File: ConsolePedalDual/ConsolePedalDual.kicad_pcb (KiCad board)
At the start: 2 copper layers, 92.3 x 90.2 mm, 14 parts, among them J1 AudioJack3, J2 AudioJack2, J3 Conn_02x25_Odd_Even, J4 Conn_02x25_Odd_Even, SW1 Bypass

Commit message: Finished schematic. Trying to figure out how to fit all these components on this board
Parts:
- removed SW1: Bypass, Connector_PinSocket_2.54mm:PinSocket_1x02_P2.54mm_Vertical
- added C1: 47uF, Capacitor_THT:CP_Radial_D6.3mm_P2.50mm, F.Cu at (232.5, 67.9)
- added C2: 2.2uF, Capacitor_THT:CP_Radial_D4.0mm_P2.00mm, F.Cu at (174.4, 78.7)
- added C3: 2.2uF, Capacitor_THT:CP_Radial_D4.0mm_P2.00mm, F.Cu at (186.2, 56.6)
- added C4: 2.2uF, Capacitor_THT:CP_Radial_D4.0mm_P2.00mm, F.Cu at (174.4, 86.0)
- added C5: 2.2uF, Capacitor_THT:CP_Radial_D4.0mm_P2.00mm, F.Cu at (186.2, 64.0)
- added C6: 2.2uF, Capacitor_THT:CP_Radial_D4.0mm_P2.00mm, F.Cu at (196.4, 71.3)
- added C7: 2.2uF, Capacitor_THT:CP_Radial_D4.0mm_P2.00mm, F.Cu at (208.1, 56.6)
- added R2: 10K, Resistor_THT:R_Axial_DIN0207_L6.3mm_D2.5mm_P10.16mm_Horizontal, F.Cu at (121.7, 94.2)
- added R3: 10K, Resistor_THT:R_Axial_DIN0207_L6.3mm_D2.5mm_P10.16mm_Horizontal, F.Cu at (207.7, 61.9)
- added R4: 510K, Resistor_THT:R_Axial_DIN0207_L6.3mm_D2.5mm_P10.16mm_Horizontal, F.Cu at (217.9, 66.0)
- added R5: 510K, Resistor_THT:R_Axial_DIN0207_L6.3mm_D2.5mm_P10.16mm_Horizontal, F.Cu at (221.1, 61.9)
- added R6: 510K, Resistor_THT:R_Axial_DIN0207_L6.3mm_D2.5mm_P10.16mm_Horizontal, F.Cu at (209.3, 76.6)
- added R7: 510K, Resistor_THT:R_Axial_DIN0207_L6.3mm_D2.5mm_P10.16mm_Horizontal, F.Cu at (196.0, 80.7)
- added R8: 510K, Resistor_THT:R_Axial_DIN0207_L6.3mm_D2.5mm_P10.16mm_Horizontal, F.Cu at (196.0, 84.7)
- added R9: 510K, Resistor_THT:R_Axial_DIN0207_L6.3mm_D2.5mm_P10.16mm_Horizontal, F.Cu at (217.9, 70.0)
- added U1: CD4053B, Package_DIP:DIP-16_W7.62mm_Socket, F.Cu at (133.3, 55.5)
- J3: value Conn_02x25_Odd_Even -> Slot A
- J4: value Conn_02x25_Odd_Even -> Slot B
- R1: value R -> LED
- moved D2 23.7 mm to (125.2, 94.0), turned to 90 degrees
- moved J2 13.3 mm to (157.7, 91.2)
- moved J1 12.6 mm to (117.3, 88.1)
- moved BT1 12.4 mm to (117.3, 79.8)
- moved D1 8.38 mm to (137.2, 77.1)
- moved R1 1.40 mm to (142.2, 83.3)
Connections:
- J3 pad 10: +9V -> /SlotA
- J3 pad 42: +9V -> /SlotA
- J3 pad 43: /SecondFX -> /SlotAOutput
- J3 pad 44: /SecondFX -> /SlotAOutput
- J3 pad 45: /Input -> /SlotAInput
- J3 pad 46: /Input -> /SlotAInput
- J3 pad 5: /Input -> /SlotAInput
- J3 pad 6: /Input -> /SlotAInput
- J3 pad 7: /SecondFX -> /SlotAOutput
- J3 pad 8: /SecondFX -> /SlotAOutput
- J4 pad 10: +9V -> /SlotB
- J4 pad 42: +9V -> /SlotB
- J4 pad 45: /SecondFX -> /SlotBInput
- J4 pad 46: /SecondFX -> /SlotBInput
- J4 pad 5: /SecondFX -> /SlotBInput
- J4 pad 6: /SecondFX -> /SlotBInput
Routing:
- net /LEDPower: track 155.5 -> 0.62 mm
- net +9V: track 147.9 -> 0.00 mm
- net /Output: track 144.2 -> 0.00 mm
- net /Input: track 131.0 -> 0.00 mm
- net /SecondFX: track 123.7 -> 0.00 mm
- net Net-(J1-Pad3): track 30.6 -> 0.00 mm
- net GND: track 30.5 -> 0.00 mm
- net Net-(J2-Pad1): track 23.4 -> 0.00 mm
- net Net-(D1-Pad1): track 16.6 -> 0.00 mm
- net Net-(BT1-Pad1): track 14.7 -> 0.00 mm
- net Net-(BT1-Pad2): track 9.33 -> 0.00 mm
- net Net-(S1-PadP$1): track 5.30 -> 0.00 mm

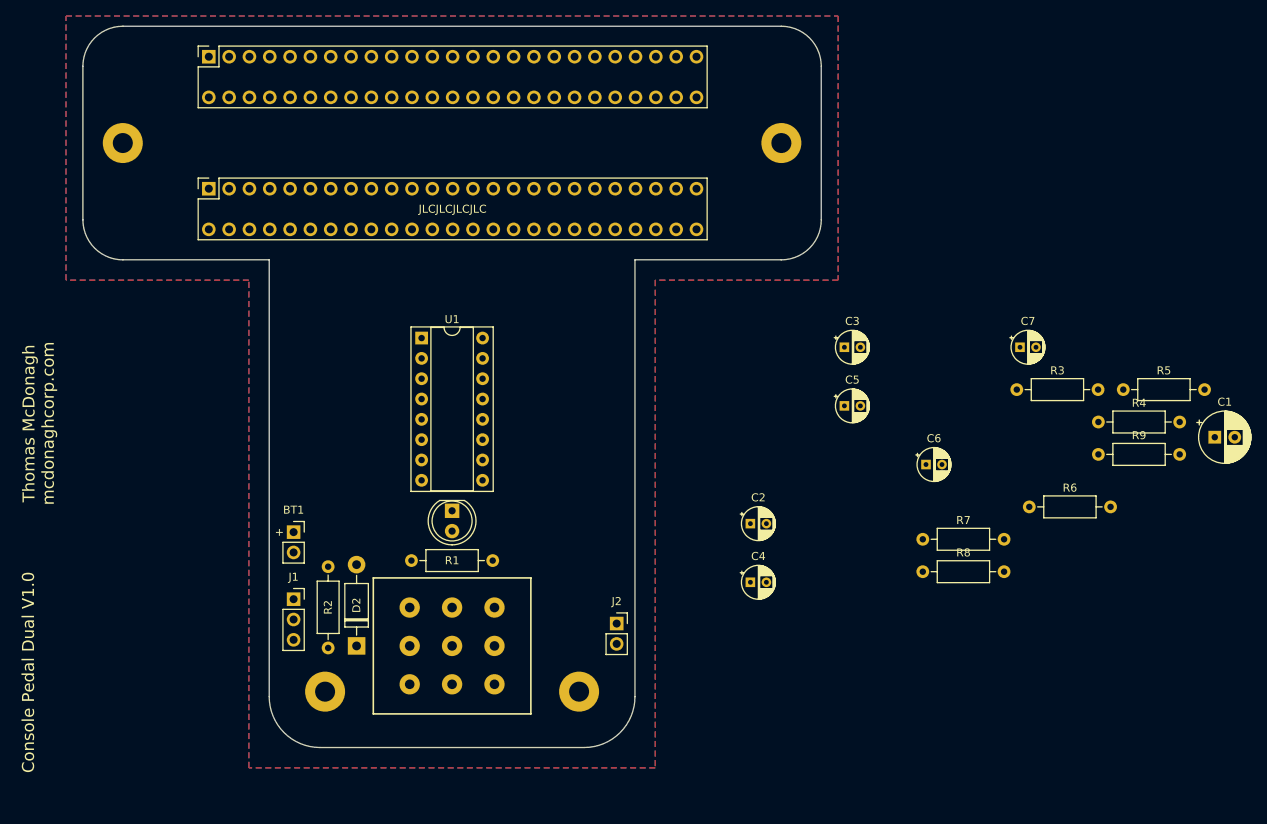
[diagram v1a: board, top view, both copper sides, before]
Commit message: Figured out how to fit components on board. Now need to add traces
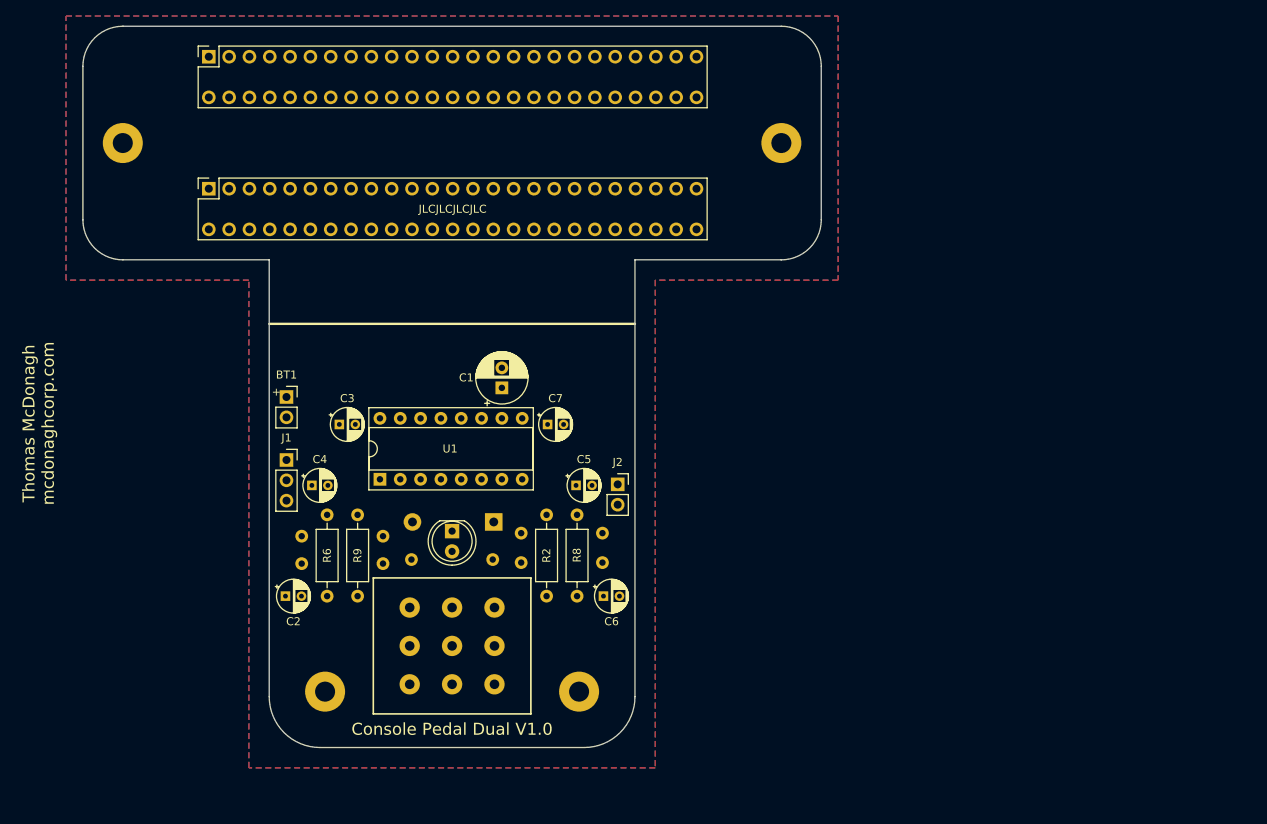
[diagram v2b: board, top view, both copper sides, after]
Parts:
- D2, R1, R3, R4, R5, R7: moved to B.Cu
- moved R5 94.3 mm to (128.5, 80.3), turned to 180 degrees
- moved R9 94.3 mm to (125.3, 87.8), turned to 90 degrees
- moved R4 91.2 mm to (128.5, 83.7), turned to 180 degrees
- moved C1 89.3 mm to (143.4, 61.7), turned to 90 degrees
- moved R6 87.8 mm to (121.5, 77.6), turned to 270 degrees
- moved C3 63.9 mm to (123.1, 66.3)
- moved C7 59.8 mm to (149.1, 66.3)
- moved C2 58.8 mm to (116.3, 87.8)
- moved C4 56.1 mm to (119.6, 73.9)
- moved R3 56.1 mm to (156.0, 83.6), turned to 180 degrees
- moved R7 50.2 mm to (145.8, 79.9)
- moved R8 43.8 mm to (152.8, 77.6), turned to 270 degrees
- moved C6 43.5 mm to (156.1, 87.8)
- moved C5 35.0 mm to (152.7, 73.9)
- moved R2 28.1 mm to (149.0, 87.8)
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
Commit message: Finalized and plotted board
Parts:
- moved D2 1.91 mm to (142.4, 76.6)
- moved D1 1.30 mm to (135.9, 79.9), turned to 0 degrees
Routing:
- net +9V: track 0.00 -> 225.0 mm, vias 0 -> 1
- net /SlotBInput: track 0.00 -> 172.4 mm, vias 0 -> 2
- net /Output: track 0.00 -> 157.8 mm
- net /LEDPower: track 0.62 -> 150.3 mm, vias 0 -> 1
- net /SlotB: track 0.00 -> 112.9 mm, vias 0 -> 1
- net /SlotAInput: track 0.00 -> 106.4 mm, vias 0 -> 1
- net /SlotAOutput: track 0.00 -> 85.8 mm
- net /VREF: track 0.00 -> 75.0 mm
- net /SlotA: track 0.00 -> 64.4 mm, vias 0 -> 1
- net Net-(C4-Pad1): track 0.00 -> 45.5 mm
- net Net-(C2-Pad1): track 0.00 -> 45.0 mm
- net Net-(C7-Pad1): track 0.00 -> 43.2 mm, vias 0 -> 2
- net Net-(J2-Pad1): track 0.00 -> 40.8 mm
- net Net-(J1-Pad3): track 0.00 -> 39.2 mm
- net Net-(C6-Pad1): track 0.00 -> 35.4 mm, vias 0 -> 1
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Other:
- board text added: "Console Pedal Dual V1.1"
- board text added: "Thomas McDonagh consolepedals.com"
- board text removed: "Console Pedal Dual V1.0"
- board text removed: "Thomas McDonagh mcdonaghcorp.com"

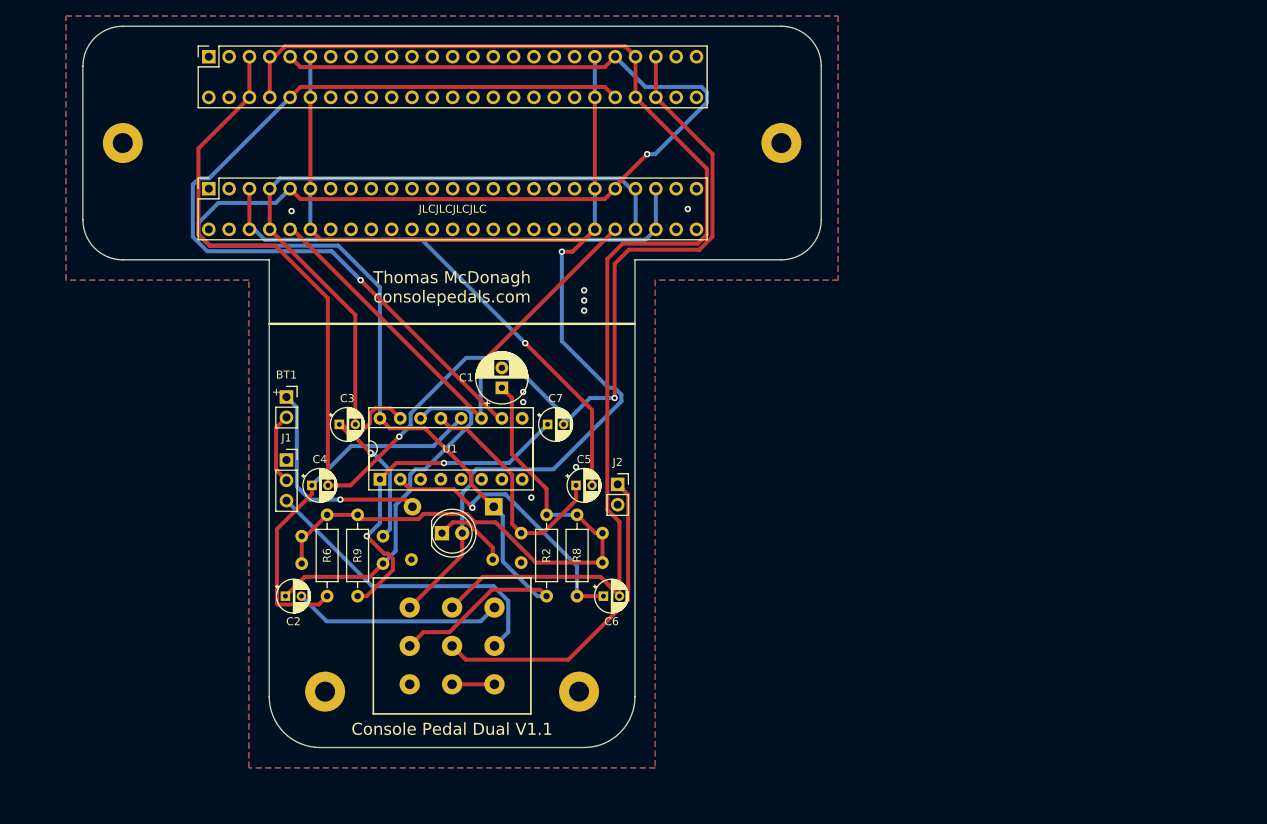
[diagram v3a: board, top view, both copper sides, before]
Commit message: Added pull down resistors, fixed mounting hole placements, and fixed 3PDT switch footprint
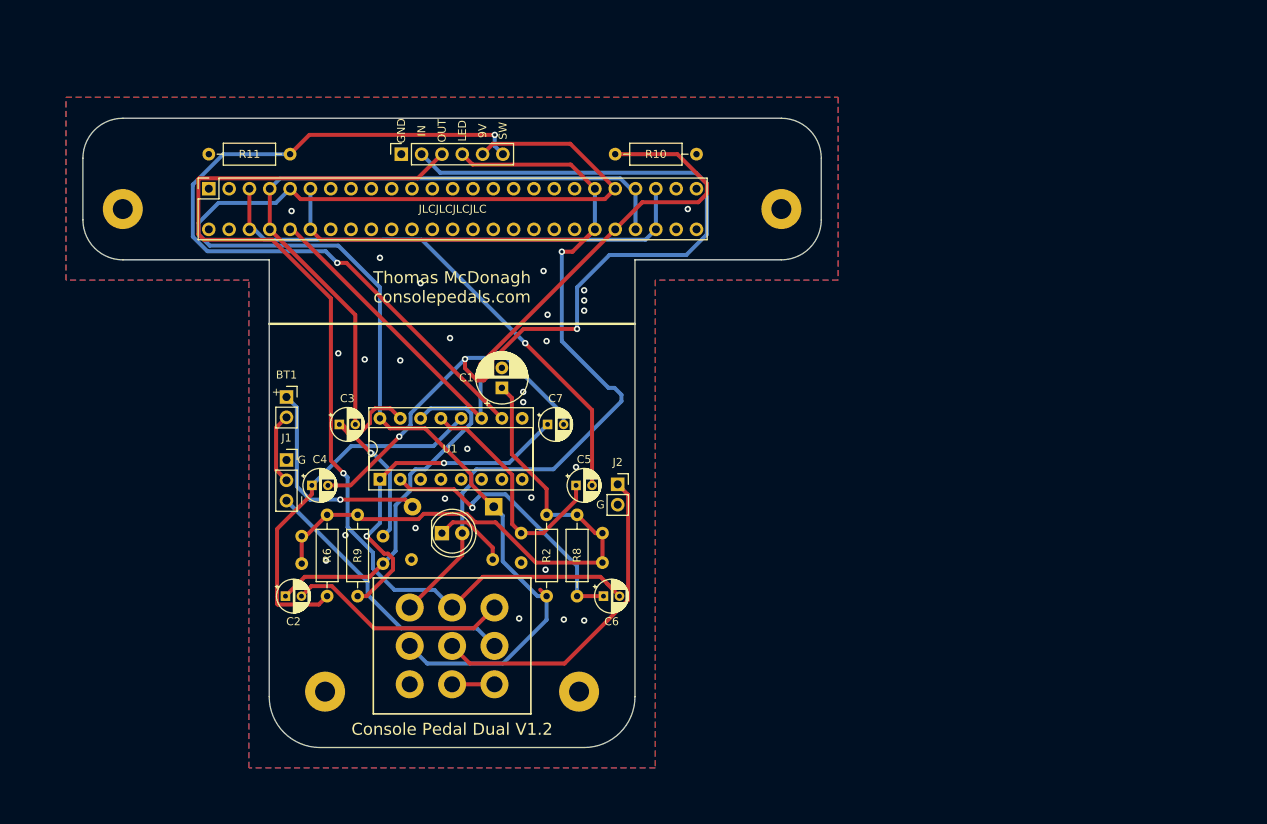
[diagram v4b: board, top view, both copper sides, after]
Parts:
- added R10: 3M, Resistor_THT:R_Axial_DIN0207_L6.3mm_D2.5mm_P10.16mm_Horizontal, F.Cu at (167.7, 32.5)
- added R11: 3M, Resistor_THT:R_Axial_DIN0207_L6.3mm_D2.5mm_P10.16mm_Horizontal, F.Cu at (116.9, 32.5)
- J4: footprint libraries:n64Socket -> Connector_PinSocket_2.54mm:PinSocket_1x06_P2.54mm_Vertical
- S1: footprint MuffPi:STOMP_SWITCH_3PDT -> libraries:STOMP_SWITCH_3PDT
- moved J4 27.0 mm to (130.8, 32.5)
- moved H1 8.25 mm to (96.0, 39.4)
- moved H3 8.25 mm to (178.3, 39.4)
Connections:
- J4 pad 2: GND -> /SlotBInput
- J4 pad 3: GND -> /Output
- J4 pad 4: GND -> /LEDPower
- J4 pad 5: /SlotBInput -> +9V
- J4 pad 6: /SlotBInput -> /SlotB
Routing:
- net +9V: track 225.0 -> 176.1 mm, vias 1 -> 0
- net /SlotBInput: track 172.4 -> 128.1 mm, vias 2 -> 3
- net /Output: track 157.8 -> 129.9 mm, vias 0 -> 1
- net /SlotA: track 64.4 -> 91.9 mm
- net /SlotB: track 112.9 -> 97.7 mm, vias 1 -> 2
- net /LEDPower: track 150.3 -> 135.7 mm
- net Net-(J1-Pad3): track 39.2 -> 34.5 mm
- net /Input: track 26.1 -> 27.9 mm
- net GND: vias 9 -> 26
- net (no net): vias 0 -> 1
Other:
- board size 92.3 x 90.2 mm -> 92.3 x 78.7 mm
- board text added: "9V"
- board text added: "Console Pedal Dual V1.2"
- board text added: "G"
- board text added: "GND"
- board text added: "I"
- board text added: "IN"
- board text added: "LED"
- board text added: "OUT"
- board text added: "SW"
- board text removed: "Console Pedal Dual V1.1"
